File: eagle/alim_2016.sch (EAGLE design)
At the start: 22 parts, among them J1 AVR_SPI_PRG_6PTH, J2 AVR_SPI_PRG_6PTH, U1 3.3V, U2 LM2678S-5.0, U3 ATMEGA328P, U4 LM2596S-ADJ, U5 ATTINY85-20SU

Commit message: thermal vias
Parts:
- added 12V: 1751248, con-phoenix-350:1751248
- added R2, R3, R4, R5: 10K, resistor:R-EU_M0805
- added S1, S2: (no value), SparkFun-Electromechanical:TAC_SWITCHPTH
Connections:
- removed net N$38: 24V-1.K, U$20.S
- new net BAT24_CUT: R2.1, S2.3, U$20.G, U3.PD2(INT0)
- new net N$12: 24V-1.K, BAT2-1.KL, R3.1
- new net N$13: BAT3-2.KL, R5.2, U$19.S
- new net N$15: R5.1, S1.1, U$19.G
- net 12V: now also 12V-1.K, BAT3-1.KL, S1.3, U2.VIN; no longer U$19.S
- net GND: now also 12V-2.K, U$19.D, U$20.D; no longer BAT1-2.KL, BAT3-2.KL
- net N$8: now also BAT1-2.KL, R2.2, R4.2, U$20.S; no longer BAT2-1.KL, U$20.D
- net N$9: now also R3.2, R4.1, S2.1; no longer BAT3-1.KL, U$19.D
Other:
- moved on the sheet: 24V-1, 24V-2, BAT1-1, BAT1-2, BAT2-1, BAT2-2, BAT3-1, BAT3-2, U$19, U$20

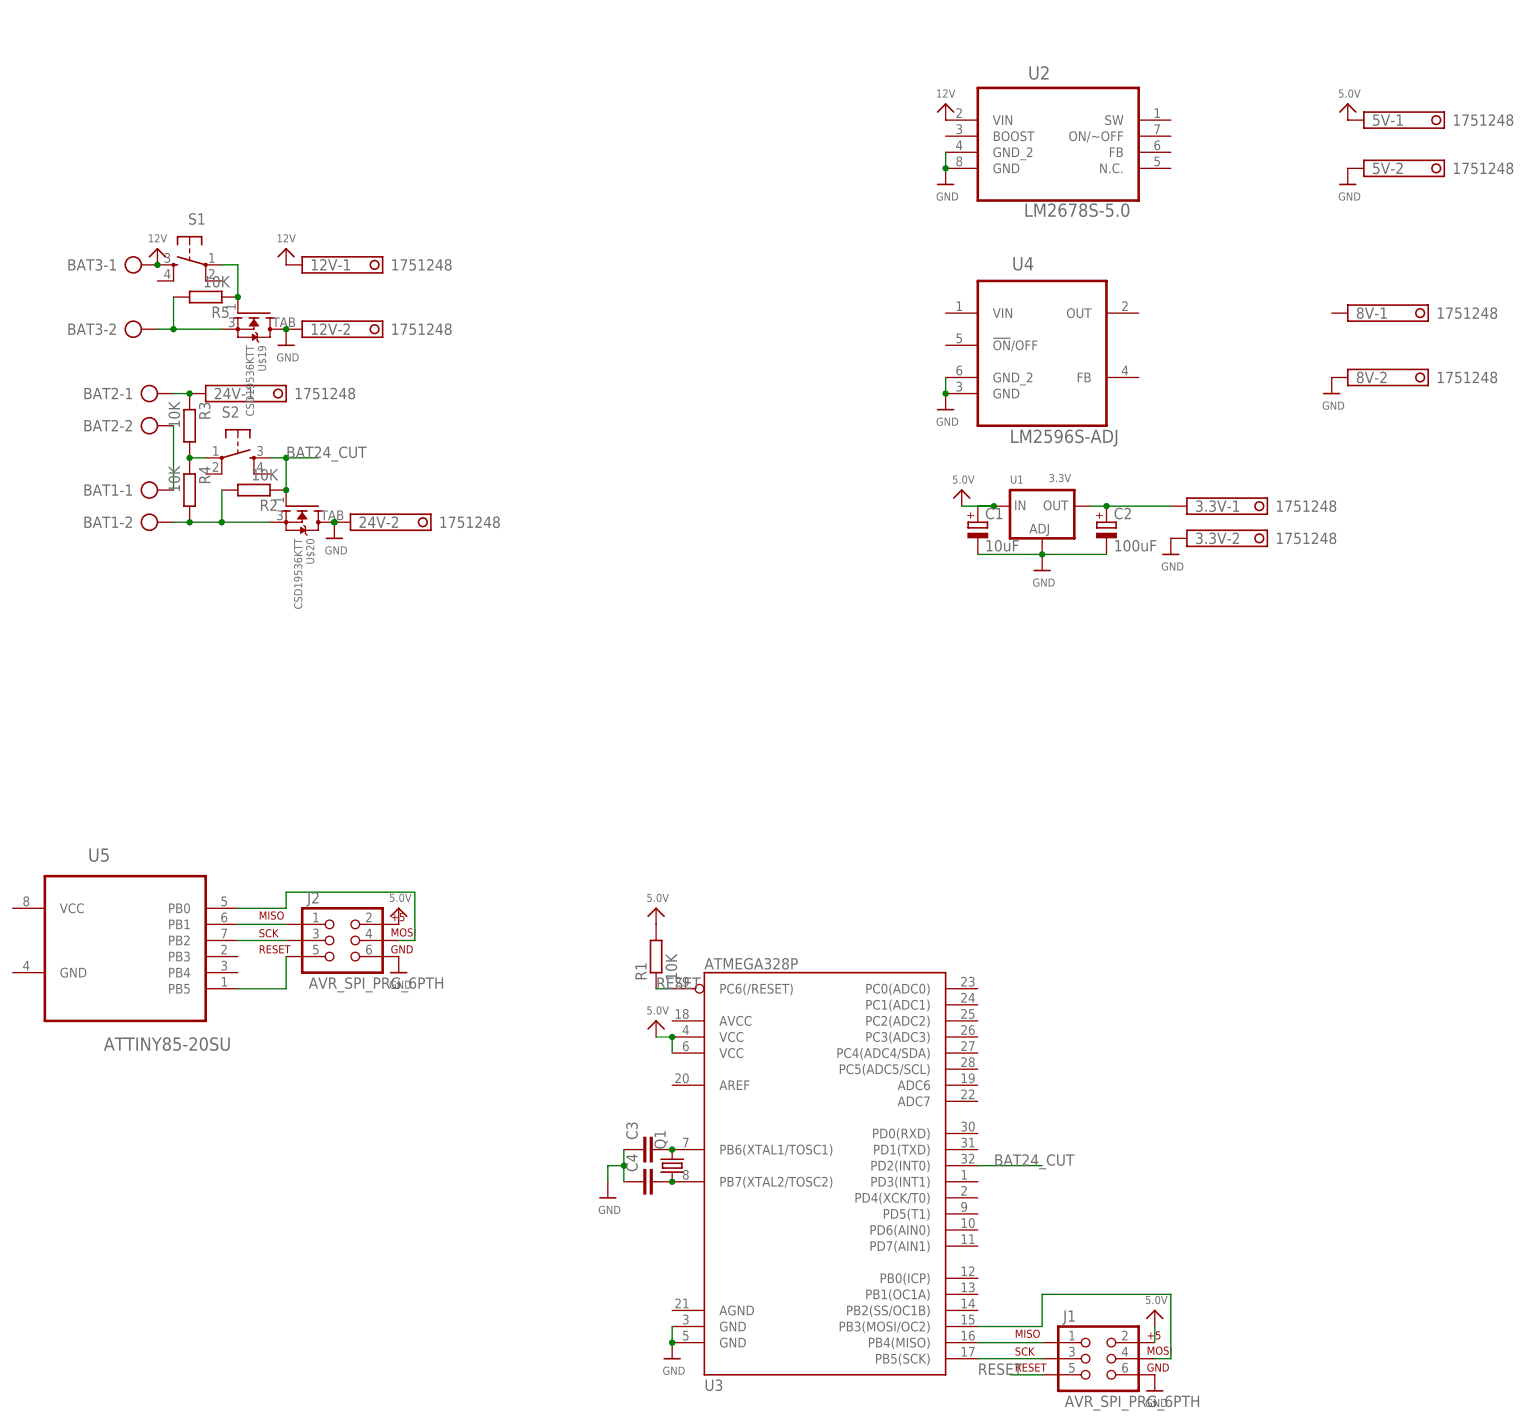
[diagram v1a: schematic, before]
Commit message: pcb rearranging
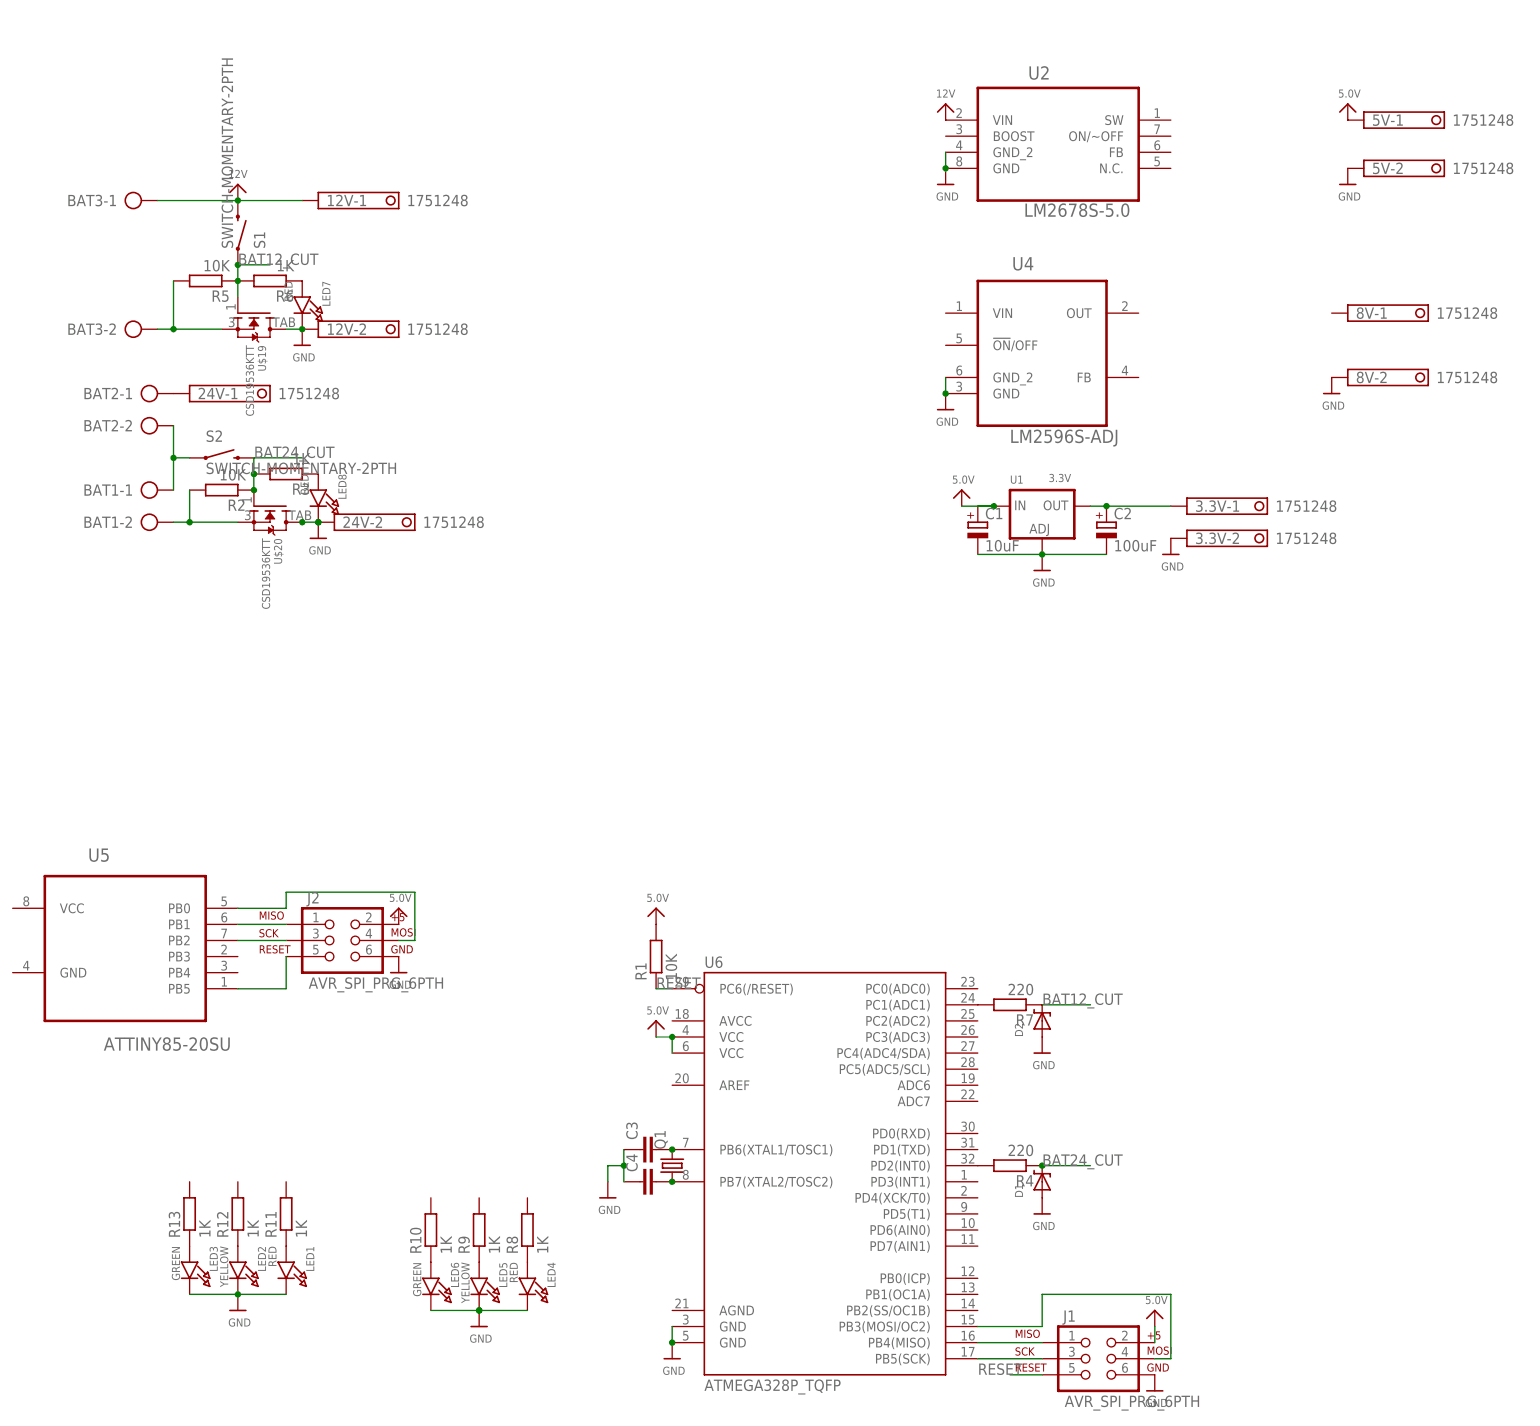
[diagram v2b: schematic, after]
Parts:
- removed U3: ATMEGA328P, SparkFun-DigitalIC:ATMEGA328_SMT
- added D1, D2: (no value), alim:DIODE-ZENERSOD123
- added LED1, LED4, LED7, LED8: RED, microbuilder:LED0805_NOOUTLINE
- added LED2, LED5: YELLOW, microbuilder:LED0805_NOOUTLINE
- added LED3, LED6: GREEN, microbuilder:LED0805_NOOUTLINE
- added R10, R11, R12, R13, R6, R8, R9: 1K, resistor:R-EU_M0805
- added R7: 220, resistor:R-EU_M0805
- added U6: ATMEGA328P_TQFP, SparkFun-DigitalIC:ATMEGA328P_TQFP
- R3: value 10K -> 1K
- R4: value 10K -> 220
- S1, S2: value (none) -> SWITCH-MOMENTARY-2PTH; device SparkFun-Electromechanical:TAC_SWITCHPTH -> SparkFun-Electromechanical:SWITCH-MOMENTARY-2PTH
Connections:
- new net BAT12_CUT: D2.C, R5.1, R6.2, R7.1, S1.1, U$19.G
- new net N$10: LED7.A, R6.1
- new net N$11: R4.2, U6.PD2(INT0)
- new net N$14: R7.2, U6.PC1(ADC1)
- new net N$16: LED5.A, R9.1
- new net N$17: LED6.A, R10.1
- new net N$18: LED1.A, R11.1
- new net N$19: LED2.A, R12.1
- new net N$20: LED3.A, R13.1
- net 12V: now also S1.2; no longer S1.3
- net 5.0V: now also U6.VCC@4, U6.VCC@6; no longer U3.VCC@1, U3.VCC@2
- net BAT24_CUT: now also D1.C, R3.2, R4.1, S2.2; no longer S2.3, U3.PD2(INT0)
- net GND: now also D1.A, D2.A, LED1.C, LED2.C, LED3.C, LED4.C, LED5.C, LED6.C, LED7.C, LED8.C, U6.GND@3, U6.GND@5; no longer U3.GND@1, U3.GND@2
- net N$12: no longer R3.1
- net N$15: now also LED4.A, R8.1; no longer R5.1, S1.1, U$19.G
- net N$2: now also U6.PB5(SCK); no longer U3.PB5(SCK)
- net N$3: now also U6.PB4(MISO); no longer U3.PB4(MISO)
- net N$4: now also U6.PB3(MOSI/OC2); no longer U3.PB3(MOSI/OC2)
- net N$5: now also S2.1
- net N$6: now also U6.PB6(XTAL1/TOSC1); no longer U3.PB6(XTAL1/TOSC1)
- net N$7: now also U6.PB7(XTAL2/TOSC2); no longer U3.PB7(XTAL2/TOSC2)
- net N$8: no longer R4.2
- net N$9: now also LED8.A, R3.1; no longer R3.2, R4.1, S2.1
- net RESET: now also U6.PC6(/RESET); no longer U3.PC6(/RESET)
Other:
- moved on the sheet: 12V-1, 12V-2, 24V-1, 24V-2, BAT3-1, R2, R3, R4, R5, U$20

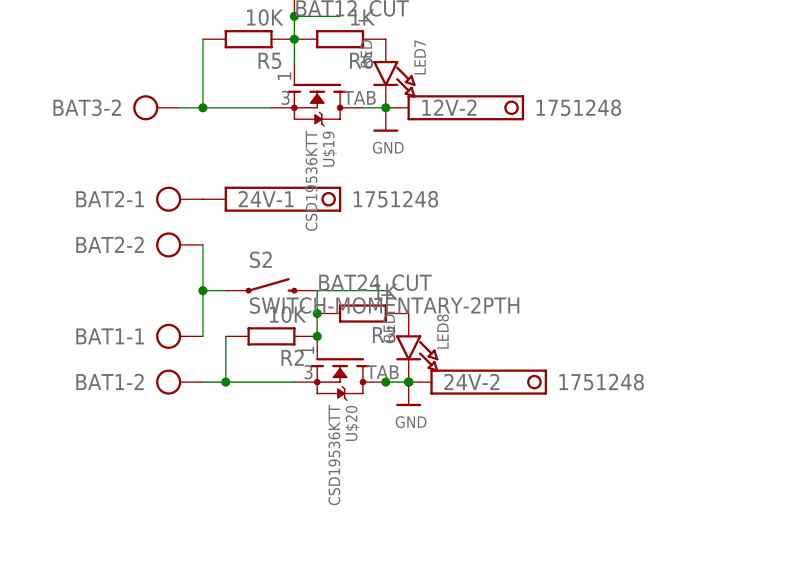
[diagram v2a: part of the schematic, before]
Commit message: remove extra switch, routing
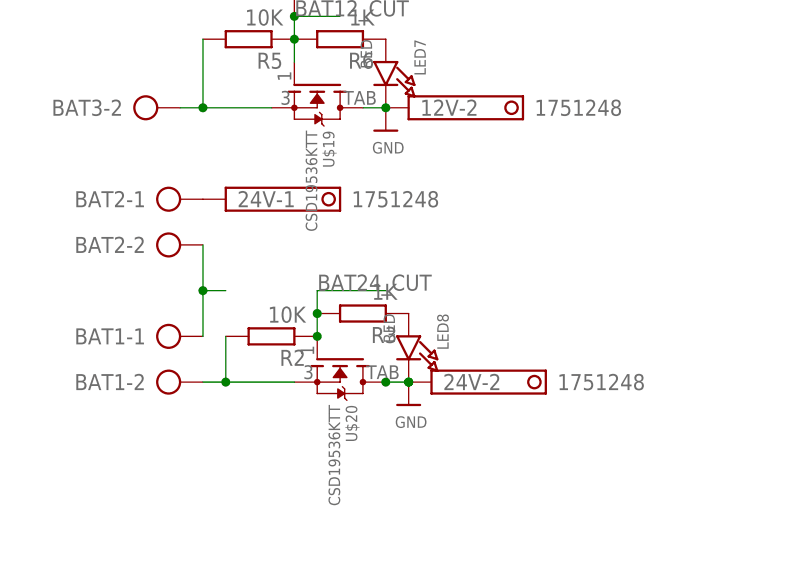
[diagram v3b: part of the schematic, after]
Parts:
- removed S2: SWITCH-MOMENTARY-2PTH, SparkFun-Electromechanical:SWITCH-MOMENTARY-2PTH
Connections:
- net BAT24_CUT: no longer S2.2
- net N$5: no longer S2.1
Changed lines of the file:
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@@
 <part name="R5" library="resistor" deviceset="R-EU_" device="M0805" value="10K"/>
 <part name="S1" library="SparkFun-Electromechanical" deviceset="SWITCH-MOMENTARY-2" device="PTH"/>
-<part name="S2" library="SparkFun-Electromechanical" deviceset="SWITCH-MOMENTARY-2" device="PTH"/>
 <part name="U$4" library="microbuilder" deviceset="12V" device=""/>
 <part name="12V" library="con-phoenix-350" deviceset="1751248" device=""/>
@@
 <instance part="R5" gate="G$1" x="-27.94" y="30.48" rot="R180"/>
 <instance part="S1" gate="G$1" x="-22.86" y="38.1" rot="MR90"/>
-<instance part="S2" gate="G$1" x="-25.4" y="2.54"/>
 <instance part="U$4" gate="G$1" x="88.9" y="58.42"/>
 <instance part="12V" gate="-1" x="-10.16" y="43.18"/>
@@
 <pinref part="BAT1" gate="-1" pin="KL"/>
 <wire x1="-33.02" y1="7.62" x2="-33.02" y2="2.54" width="0.1524" layer="91"/>
-<pinref part="S2" gate="G$1" pin="1"/>
 <wire x1="-33.02" y1="2.54" x2="-33.02" y2="-2.54" width="0.1524" layer="91"/>
 <wire x1="-30.48" y1="2.54" x2="-33.02" y2="2.54" width="0.1524" layer="91"/>
@@
 <junction x="-20.32" y="-2.54"/>
 <wire x1="-20.32" y1="-2.54" x2="-20.32" y2="0" width="0.1524" layer="91"/>
-<pinref part="S2" gate="G$1" pin="2"/>
 <wire x1="-20.32" y1="2.54" x2="-20.32" y2="0" width="0.1524" layer="91"/>
 <label x="-20.32" y="2.54" size="1.778" layer="95"/>
